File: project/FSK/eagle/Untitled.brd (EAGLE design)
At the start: 120 x 74 mm, 20 parts, among them X1 SMA-142-0711-821/826, X2 SMA-142-0711-821/826, X3 SMA-142-0711-821/826, X4 SMA-142-0711-821/826, X5 SMA-142-0711-821/826

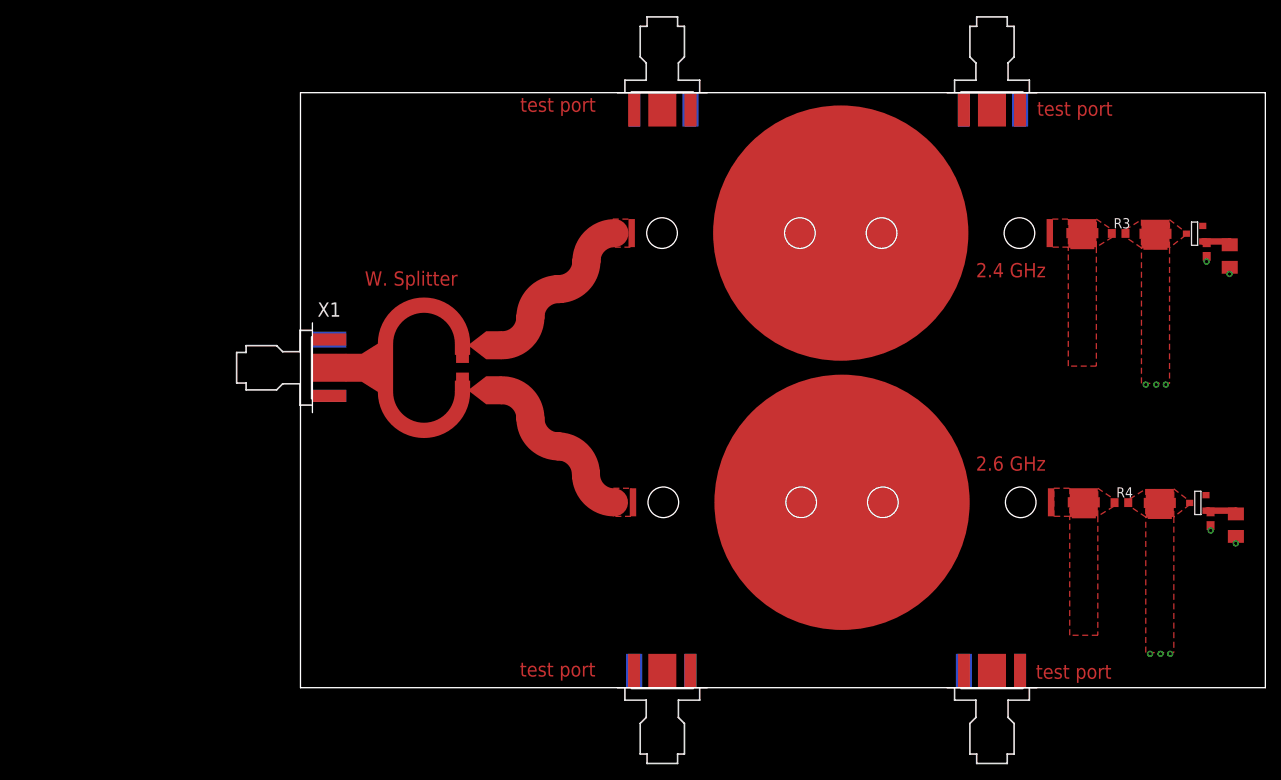
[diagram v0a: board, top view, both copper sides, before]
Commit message: added FSK version 2
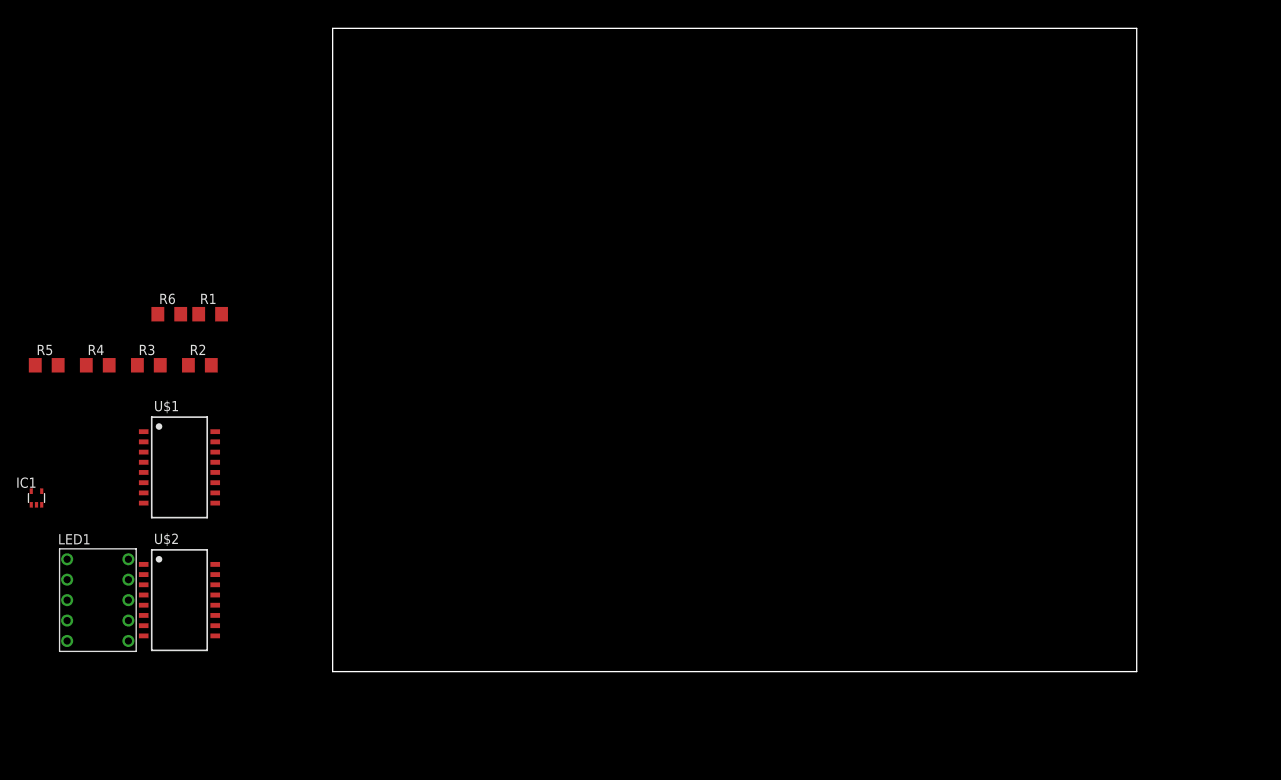
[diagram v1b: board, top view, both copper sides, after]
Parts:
- removed 2.4FIL, 2.4TUNED, 2.6FIL, 2.6TUNED: TEE_TL1, ECE532_Parts:TEE_TL1
- removed C1, C2: 100 pF, rcl:C0603
- removed FILTER1: 2.4GHz, ECE532_Parts:1IN_PIPE_CAP
- removed FILTER2: 2.6GHz, ECE532_Parts:1IN_PIPE_CAP
- removed U$3: HSMS-2850, ECE532_Parts:HSMS-2850
- removed X1, X2, X3, X4, X5: SMA-142-0711-821/826, con-coax:J502-ND-142-0711-821/826
- added IC1: 74AUC1G32DCK, 74xx-little-de:SC70-5
- added LED1: S4301B, led-7-segment:S4301B
- added R5: 4.7k, rcl:R1206
- added R6: 10k, rcl:R1206
- R1: device rcl:M1206 -> rcl:R1206
- R2: value 10k -> 4.7k; device rcl:M1206 -> rcl:R1206
- R3, R4: value (none) -> 4.7k; device rcl:R0603 -> rcl:R1206
- U$1: value WSPLITTER_2.5GHZ -> CD54HC4511; device ECE532_Parts:WSPLITTER_2.5GHZ -> ECE532_Parts:CD54HC4511
- U$2: value HSMS-2850 -> TSM983ESE+T; device ECE532_Parts:HSMS-2850 -> ECE532_Parts:TSM983ESE+T
- moved U$2 134.2 mm to (-19.1, 8.89), turned to 0 degrees
- moved R2 130.4 mm to (-16.5, 38.1), turned to 0 degrees
- moved R4 128.4 mm to (-29.2, 38.1)
- moved R1 127.0 mm to (-15.2, 44.5), turned to 0 degrees
- moved R3 121.7 mm to (-22.9, 38.1)
- moved U$1 32.6 mm to (-19.1, 26.7)
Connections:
- removed net 2.4FIL: 2.4FIL.T_B, 2.4FIL.T_L, 2.4FIL.T_R, FILTER1.OUT, R3.1
- removed net 2.4GHZ: FILTER1.IN, U$1.P$2
- removed net 2.4TUNED: 2.4TUNED.T_B, 2.4TUNED.T_L, 2.4TUNED.T_R, R3.2, U$2.A
- removed net 2.6FIL: 2.6FIL.T_B, 2.6FIL.T_L, 2.6FIL.T_R, FILTER2.OUT, R4.1
- removed net 2.6GHZ: FILTER2.IN, U$1.P$3
- removed net 2.6TUNED: 2.6TUNED.T_B, 2.6TUNED.T_L, 2.6TUNED.T_R, R4.2, U$3.A
- removed net GND1: C1.2, C2.2, R1.1, R2.1, X1.G@1, X1.G@2, X1.G@3, X1.G@4
- new net AGND: IC1.3, LED1.3, LED1.8, R3.1, R5.1, R6.1, U$1.1, U$1.2, U$1.5, U$1.6, U$1.8, U$2.12, U$2.13, U$2.14, U$2.9
- new net N$1: IC1.1, U$2.1
- new net N$10: R2.2, R4.2, U$2.8
- new net N$11: LED1.7, U$1.11
- new net N$12: LED1.9, U$1.12
- new net N$13: LED1.10, U$1.13
- new net N$14: LED1.1, U$1.14
- new net N$15: LED1.2, U$1.15
- new net N$2: R1.1, U$1.3
- new net N$6: U$1.7, U$2.2
- new net N$7: R2.1, R3.2, U$2.4, U$2.6
- new net N$8: LED1.4, U$1.9
- new net N$9: LED1.5, U$1.10
- new net VCC: IC1.5, R1.2, U$1.16, U$2.3
- net N$3: now also IC1.4, R6.2, U$1.4; no longer C1.1, R1.2, U$2.C
- net N$4: now also IC1.2, U$2.16; no longer C2.1, R2.2, U$3.C
- net N$5: now also R4.1, R5.2, U$2.10; no longer U$1.P$1, X1.1
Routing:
- net 2.6GHZ: track 9.87 -> 0.00 mm
- net 2.4GHZ: track 9.87 -> 0.00 mm
- net N$4: track 4.12 -> 0.00 mm
- net N$3: track 3.77 -> 0.00 mm
- removed copper zone on layer 1, net 2.4FIL
- removed copper zone on layer 1, net 2.4GHZ
- removed copper zone on layer 1, net 2.4TUNED
- removed copper zone on layer 1, net 2.6FIL
- removed copper zone on layer 1, net 2.6GHZ
- removed copper zone on layer 1, net 2.6TUNED
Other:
- board size 120 x 74 mm -> 100 x 80 mm
- board text removed: "2.4 GHz"
- board text removed: "2.6 GHz"
- board text removed: "W. Splitter"
- board text removed: "test port"
